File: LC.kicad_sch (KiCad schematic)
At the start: 81 parts, among them J1 INPUT+, J10 DISPLAY, J11 MODE_BUTTON, J12 CAL_BUTTON, J2 INPUT-, J3 Barrel_Jack, J4 EXT_CLK, J5 CLKSRC, J6 SIGSRC, J7 EXT_SIG, J8 Conn_01x06_Male, J9 PROG, Q1 BC817, Q2 BC817, SW1 RESET_BTN, U1 Omron_G2V, U10 74HC590PW,118, U11 74HCS251, U12 AVR32DB28x-xSO, U2 L7805, U3 74AHC1G04, U4 Omron_G2E, U5 74AHC1G14, U6 74AHC1G04, U7 LM311, U8 74AUC1G74, U9 74AUC2G125, Y1 10MHz

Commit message: update display connector
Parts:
- removed J10: DISPLAY, Connector_PinHeader_2.54mm:PinHeader_1x05_P2.54mm_Vertical, symbol Connector:Conn_01x05_Male
- added J10: DISPLAY, Connector_PinHeader_2.54mm:PinHeader_1x04_P2.54mm_Vertical, symbol Connector:Conn_01x04_Male
- renumbered C20 to C19, C21 to C20, C22 to C21, C23 to C22, C24 to C23, C25 to C24, C26 to C25, C27 to C26, C28 to C27
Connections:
- net +5V: now also J10.2 (Pin_2)
- net DISP/SDA: now also J10.3 (Pin_3)
- net DISP/SDC: now also J10.4 (Pin_4)
- net GND: now also J10.1 (Pin_1)
- net DISP/SS renamed UNUSED_6

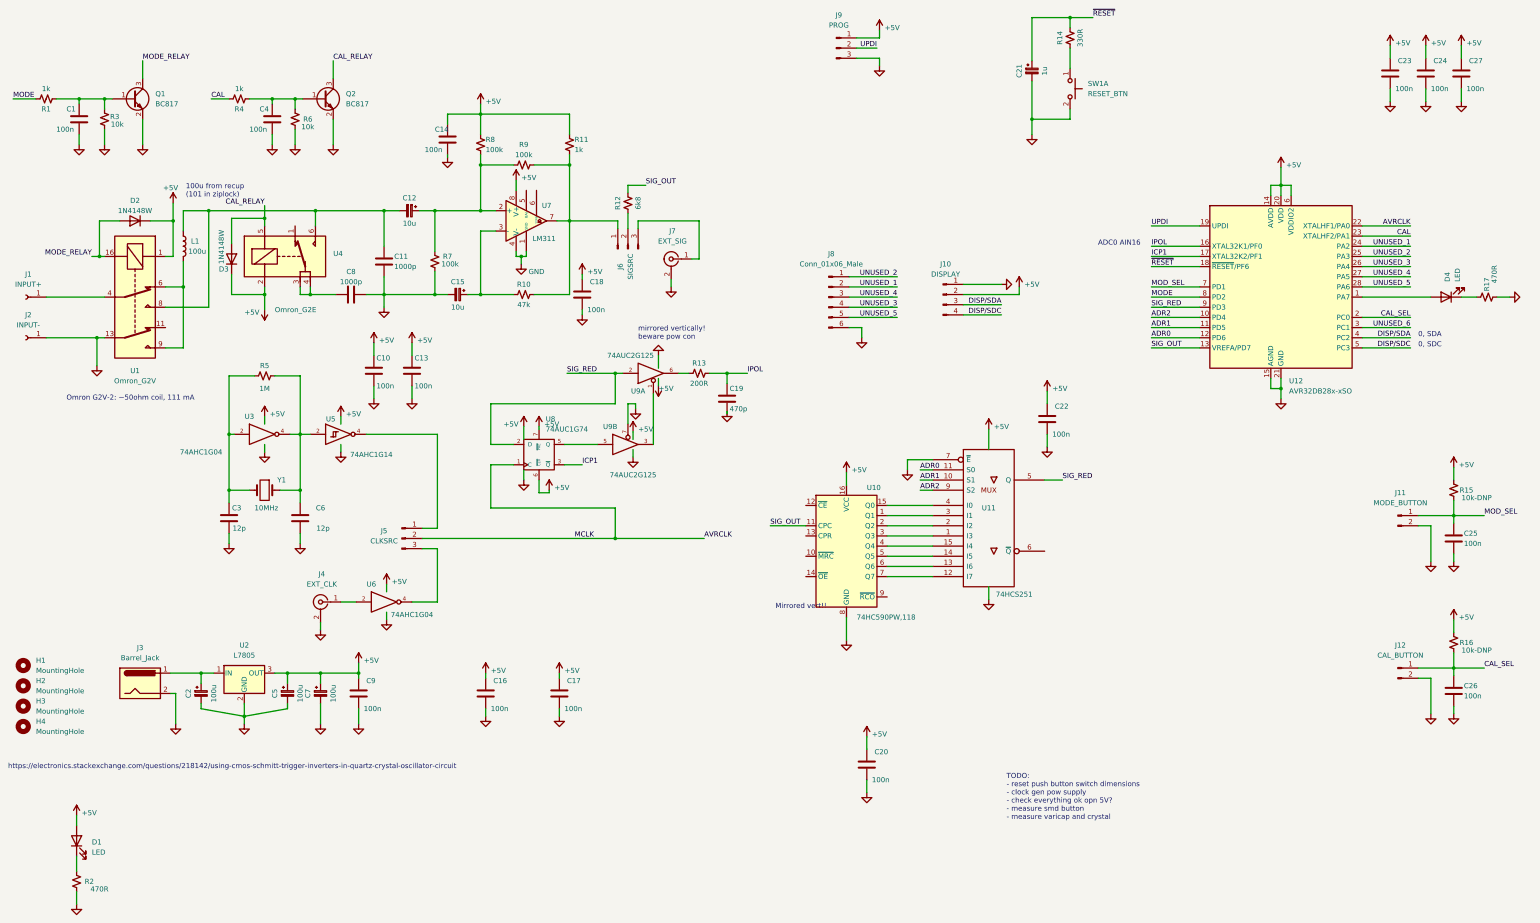
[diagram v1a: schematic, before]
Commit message: Unused IO to connector and LCD connector
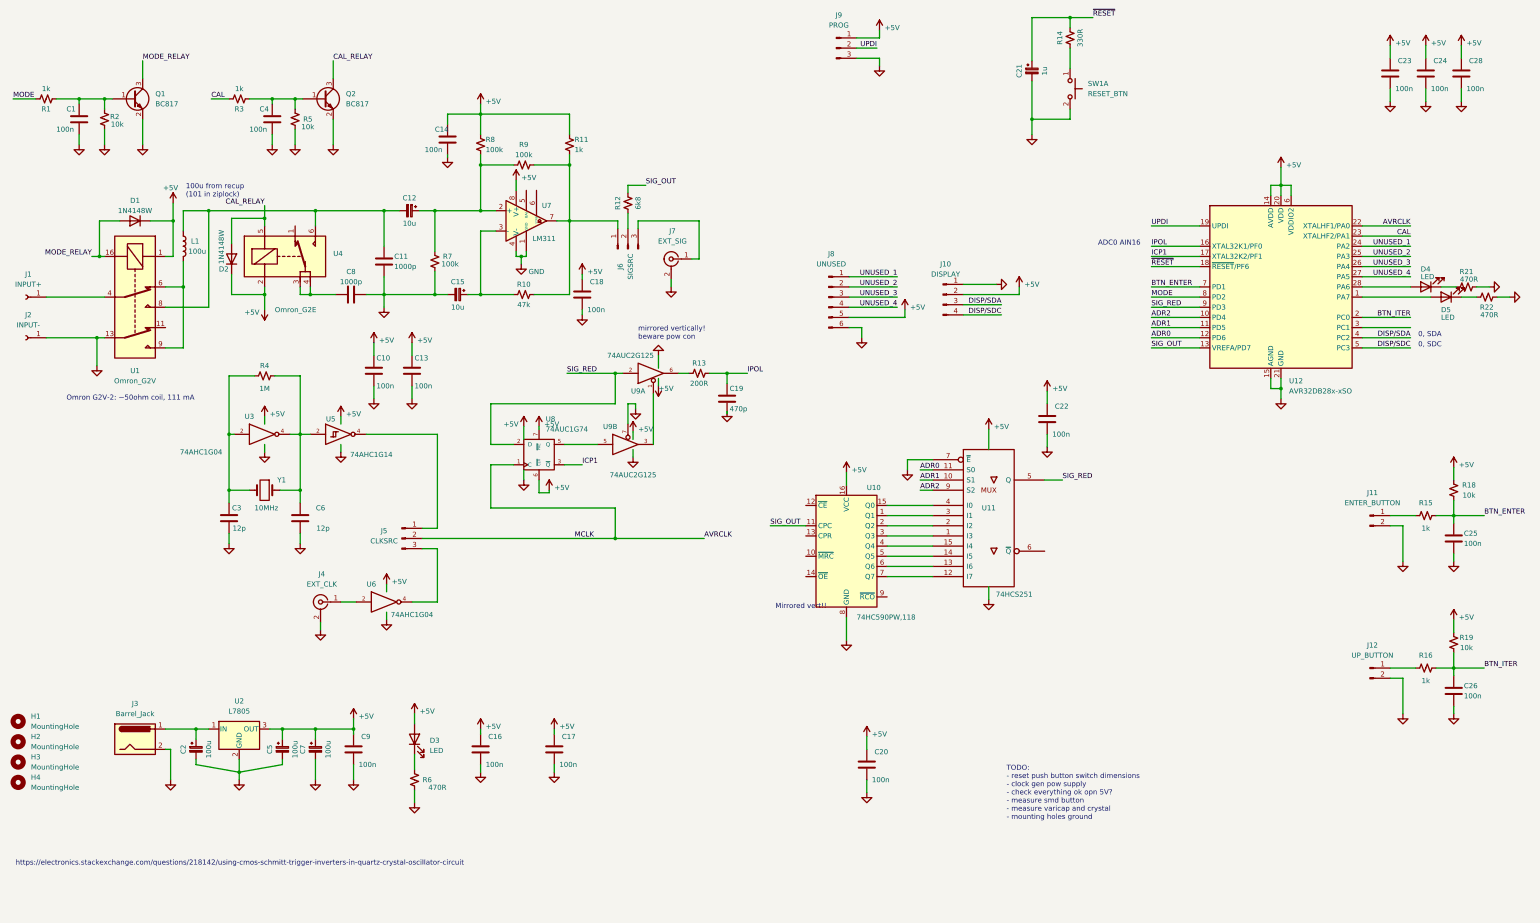
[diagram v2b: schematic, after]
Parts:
- added D4: LED, LED_SMD:LED_1206_3216Metric, symbol Device:LED
- added R15, R16: 1k, Resistor_SMD:R_0805_2012Metric_Pad1.20x1.40mm_HandSolder, symbol Device:R_Small_US
- added R21: 470R, Resistor_SMD:R_0805_2012Metric_Pad1.20x1.40mm_HandSolder, symbol Device:R_Small_US
- J11: value MODE_BUTTON -> ENTER_BUTTON
- J12: value CAL_BUTTON -> UP_BUTTON
- J8: value Conn_01x06_Male -> UNUSED
- R18: renamed from R15; value 10k-DNP -> 10k
- R19: renamed from R16; value 10k-DNP -> 10k
- renumbered C27 to C28, D2 to D1, D3 to D2, D1 to D3, D4 to D5, R3 to R2, R17 to R22, R4 to R3, R5 to R4, R6 to R5, R2 to R6
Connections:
- net +5V: now also J8.5 (Pin_5)
- net GND: now also R21.2
- net UNUSED_1: now also J8.1 (Pin_1); no longer J8.2 (Pin_2)
- net UNUSED_2: now also J8.2 (Pin_2); no longer J8.1 (Pin_1)
- net UNUSED_3: now also J8.3 (Pin_3); no longer J8.4 (Pin_4)
- net UNUSED_4: now also J8.4 (Pin_4); no longer J8.3 (Pin_3)
- net CAL_SEL renamed BTN_ITER
- net BTN_ITER: now also R16.2; no longer J12.1 (Pin_1)
- net MOD_SEL renamed BTN_ENTER
- net BTN_ENTER: now also R15.2; no longer J11.1 (Pin_1)
- net UNUSED_5: no longer names the net of U12.28 (PA6)
- net UNUSED_5: now also D4.2 (A); no longer J8.5 (Pin_5)
- net UNUSED_6: no longer names the net of U12.3 (PC1)
- new net: J12.1 (Pin_1), R16.1
- new net: J11.1 (Pin_1), R15.1
- new net: D4.1 (K), R21.1
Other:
- note added: "TODO: - reset push button switch dimensions - clock gen pow supply - check everything ok opn 5V? - measure smd button - measure varicap and crystal - mounting holes ground"
- note removed: "TODO: - reset push button switch dimensions - clock gen pow supply - check everything ok opn 5V? - measure smd button - measure varicap and crystal"
- moved on the sheet: C16, C17, C2, C5, C7, C9, D3, H1, H2, H3, H4, J11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

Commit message: update gitignore and init code
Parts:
- added TP1: TestPoint, TestPoint:TestPoint_THTPad_1.0x1.0mm_Drill0.5mm, symbol Connector:TestPoint
- renumbered C28 to C27, R18 to R17, R19 to R18, R21 to R19, R22 to R20
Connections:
- net LED_2: now reaches D5.2 (A), U12.1 (PA7)
- net LED_1: now reaches D4.2 (A), U12.28 (PA6)
- net UNUSED_5: now reaches U12.3 (PC1)
- net UNUSED_5: now also TP1.1

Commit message: changed comparator: LM311 became TLV3201
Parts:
- removed U7: LM311, Package_SO:SOIC-8-1EP_3.9x4.9mm_P1.27mm_EP2.41x3.3mm, symbol Comparator:LM311
- added U10: TLV3201, Package_TO_SOT_SMD:SOT-23-5, symbol Comparator:TLV7031DBV
- renumbered U10 to U11, U11 to U12, U12 to U13
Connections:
- net +5V: now also U10.5 (V+)
- net GND: now also U10.2 (V-)
- net IN+: now reaches C12.1, R7.2, R8.1, R9.1
- net IN+: now also U10.3 (+)
- net IN-: now reaches C15.1, R10.1
- net IN-: now also U10.4 (-)
- net COMP_OUT: now reaches J6.1 (Pin_1), R10.2, R11.1, R9.2
- net COMP_OUT: now also U10.1
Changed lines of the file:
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@@
   (junction (at 93.98 66.675) (diameter 0) (color 0 0 0 0)
   )
-  (junction (at 145.415 78.105) (diameter 0) (color 0 0 0 0)
-  )
   (junction (at 123.825 66.675) (diameter 0) (color 0 0 0 0)
   )
@@
     (stroke (width 0) (type default) (color 0 0 0 0))
   )
-  (wire (pts (xy 146.685 78.105) (xy 145.415 78.105))
-    (stroke (width 0) (type default) (color 0 0 0 0))
-  )
   (wire (pts (xy 187.96 78.74) (xy 189.865 78.74))
     (stroke (width 0) (type default) (color 0 0 0 0))
@@
     (stroke (width 0) (type default) (color 0 0 0 0))
   )
-  (wire (pts (xy 145.415 78.105) (xy 144.145 78.105))
-    (stroke (width 0) (type default) (color 0 0 0 0))
-  )
   (wire (pts (xy 85.725 203.835) (xy 85.725 205.105))
     (stroke (width 0) (type default) (color 0 0 0 0))
@@
     (stroke (width 0) (type default) (color 0 0 0 0))
   )
-  (wire (pts (xy 145.415 78.105) (xy 145.415 80.01))
+  (wire (pts (xy 144.145 76.835) (xy 144.145 78.74))
     (stroke (width 0) (type default) (color 0 0 0 0))
   )
@@
     (stroke (width 0) (type default) (color 0 0 0 0))
   )
-  (wire (pts (xy 144.145 78.105) (xy 144.145 76.835))
-    (stroke (width 0) (type default) (color 0 0 0 0))
-  )
   (wire (pts (xy 367.665 78.105) (xy 355.6 78.105))
     (stroke (width 0) (type default) (color 0 0 0 0))
@@
     (stroke (width 0) (type default) (color 0 0 0 0))
   )
-  (wire (pts (xy 146.685 76.835) (xy 146.685 78.105))
-    (stroke (width 0) (type default) (color 0 0 0 0))
-  )
   (wire (pts (xy 239.395 88.265) (xy 227.33 88.265))
     (stroke (width 0) (type default) (color 0 0 0 0))
@@
     (effects (font (size 1.27 1.27)) (justify left bottom))
   )
+  (label "IN-" (at 136.525 71.755 0)
+    (effects (font (size 1.27 1.27)) (justify left bottom))
+  )
   (label "SIG_OUT" (at 176.53 60.325 0)
     (effects (font (size 1.27 1.27)) (justify left bottom))
@@
     (effects (font (size 1.27 1.27)) (justify left bottom))
   )
+  (label "IN+" (at 136.525 66.675 0)
+    (effects (font (size 1.27 1.27)) (justify left bottom))
+  )
   (label "UNUSED_1" (at 367.665 75.565 180)
     (effects (font (size 1.27 1.27)) (justify right bottom))
@@
     (effects (font (size 1.27 1.27)) (justify right bottom))
   )
+  (label "COMP_OUT" (at 154.94 69.215 0)
+    (effects (font (size 1.27 1.27)) (justify left bottom))
+  )
   (label "MODE_RELAY" (at 38.1 78.105 180)
     (effects (font (size 1.27 1.27)) (justify right bottom))
@@
     (pin "1")
   )
-  (symbol (lib_id "power:GND") (at 145.415 80.01 0) (unit 1)
+  (symbol (lib_id "power:GND") (at 144.145 78.74 0) (unit 1)
     (in_bom yes) (on_board yes)
-    (property "Reference" "#PWR036" (id 0) (at 145.415 86.36 0)
+    (property "Reference" "#PWR036" (id 0) (at 144.145 85.09 0)
       (effects (font (size 1.27 1.27)) hide)
     )
-    (property "Value" "GND" (id 1) (at 149.225 81.915 0))
-    (property "Footprint" "" (id 2) (at 145.415 80.01 0)
+    (property "Value" "GND" (id 1) (at 147.955 80.645 0))
+    (property "Footprint" "" (id 2) (at 144.145 78.74 0)
       (effects (font (size 1.27 1.27)) hide)
     )
-    (property "Datasheet" "" (id 3) (at 145.415 80.01 0)
+    (property "Datasheet" "" (id 3) (at 144.145 78.74 0)
       (effects (font (size 1.27 1.27)) hide)
     )
@@
   (symbol (lib_id "74xx_IEEE:74251") (at 262.255 142.875 0) (unit 1)
     (in_bom yes) (on_board yes)
-    (property "Reference" "U11" (id 0) (at 262.255 140.97 0))
+    (property "Reference" "U12" (id 0) (at 262.255 140.97 0))
     (property "Value" "74HCS251" (id 1) (at 268.605 162.56 0))
     (property "Footprint" "Package_SO:SOIC-16_4.55x10.3mm_P1.27mm" (id 2) (at 262.255 142.875 0)
@@
     (pin "2")
   )
+  (symbol (lib_id "Comparator:TLV7031DBV") (at 146.685 69.215 0) (unit 1)
+    (in_bom yes) (on_board yes)
+    (property "Reference" "U10" (id 0) (at 146.685 61.595 0))
+    (property "Value" "TLV3201" (id 1) (at 149.225 64.135 0))
+    (property "Footprint" "Package_TO_SOT_SMD:SOT-23-5" (id 2) (at 144.145 74.295 0)
+      (effects (font (size 1.27 1.27)) (justify left) hide)
+    )
+    (property "Datasheet" "https://www.ti.com/lit/ds/symlink/tlv7031.pdf" (id 3) (at 146.685 64.135 0)
+      (effects (font (size 1.27 1.27)) hide)
+    )
+    (pin "2")
+    (pin "5")
+    (pin "1")
+    (pin "3")
+    (pin "4")
+  )
   (symbol (lib_id "Device:C_Polarized_Small") (at 117.475 66.675 270) (unit 1)
     (in_bom yes) (on_board yes)
@@
   (symbol (lib_id "MCU_Microchip_AVR_Dx:AVR32DB28x-xSO") (at 335.28 85.725 0) (unit 1)
     (in_bom yes) (on_board yes) (fields_autoplaced)
-    (property "Reference" "U12" (id 0) (at 337.2994 109.22 0)
+    (property "Reference" "U13" (id 0) (at 337.2994 109.22 0)
       (effects (font (size 1.27 1.27)) (justify left))
     )
@@
   (symbol (lib_id "74xx:74HC590") (at 226.695 153.035 0) (unit 1)
     (in_bom yes) (on_board yes)
-    (property "Reference" "U10" (id 0) (at 231.775 135.89 0)
+    (property "Reference" "U11" (id 0) (at 231.775 135.89 0)
       (effects (font (size 1.27 1.27)) (justify left))
     )
@@
     (pin "1")
   )
-  (symbol (lib_id "Comparator:LM311") (at 146.685 69.215 0) (unit 1)
-    (in_bom yes) (on_board yes)
-    (property "Reference" "U7" (id 0) (at 151.765 65.405 0))
-    (property "Value" "LM311" (id 1) (at 151.13 73.66 0))
-    (property "Footprint" "Package_SO:SOIC-8-1EP_3.9x4.9mm_P1.27mm_EP2.41x3.3mm" (id 2) (at 146.685 69.215 0)
-      (effects (font (size 1.27 1.27)) hide)
-    )
-    (property "Datasheet" "https://www.st.com/resource/en/datasheet/lm311.pdf" (id 3) (at 146.685 69.215 0)
-      (effects (font (size 1.27 1.27)) hide)
-    )
-    (pin "1")
-    (pin "2")
-    (pin "3")
-    (pin "4")
-    (pin "5")
-    (pin "6")
-    (pin "7")
-    (pin "8")
-  )
   (symbol (lib_id "power:+5V") (at 152.4 136.525 0) (unit 1)
     (in_bom yes) (on_board yes)
@@
       (reference "U6") (unit 1) (value "74AHC1G04") (footprint "Package_TO_SOT_SMD:SOT-23-5_HandSoldering")
     )
-    (path "/e2f067f1-c989-43ab-9cfa-23c1f9e18b39"
-      (reference "U7") (unit 1) (value "LM311") (footprint "Package_SO:SOIC-8-1EP_3.9x4.9mm_P1.27mm_EP2.41x3.3mm")
-    )
     (path "/bdc82b14-9cfe-4a26-bfe3-09c093fb2345"
       (reference "U8") (unit 1) (value "74AUC1G74") (footprint "Package_SO:VSSOP-8_2.3x2mm_P0.5mm")
@@
       (reference "U9") (unit 2) (value "74AUC2G125") (footprint "Package_SO:VSSOP-8_2.4x2.1mm_P0.5mm")
     )
+    (path "/1aff49b6-bd0b-404b-bd3a-71b68a68ad3b"
+      (reference "U10") (unit 1) (value "TLV3201") (footprint "Package_TO_SOT_SMD:SOT-23-5")
+    )
     (path "/be55dabe-c026-4082-96e0-5f65c839136b"
-      (reference "U10") (unit 1) (value "74HC590PW,118") (footprint "Package_SO:TSSOP-16_4.4x5mm_P0.65mm")
+      (reference "U11") (unit 1) (value "74HC590PW,118") (footprint "Package_SO:TSSOP-16_4.4x5mm_P0.65mm")
     )
     (path "/10bd52e6-af6a-413e-9c10-f3da44c4133b"
-      (reference "U11") (unit 1) (value "74HCS251") (footprint "Package_SO:SOIC-16_4.55x10.3mm_P1.27mm")
+      (reference "U12") (unit 1) (value "74HCS251") (footprint "Package_SO:SOIC-16_4.55x10.3mm_P1.27mm")
     )
     (path "/8b3913bb-73bc-468d-a4a4-eaf44e1d1389"
-      (reference "U12") (unit 1) (value "AVR32DB28x-xSO") (footprint "Package_SO:SOIC-28W_7.5x17.9mm_P1.27mm")
+      (reference "U13") (unit 1) (value "AVR32DB28x-xSO") (footprint "Package_SO:SOIC-28W_7.5x17.9mm_P1.27mm")
     )
     (path "/933c2574-012e-47d3-94dd-3c3fcd695e78"

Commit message: R11 is Do Not Populate
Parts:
- R11: value 1k -> 1k DNP
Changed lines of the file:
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@@
       (effects (font (size 1.27 1.27)) (justify right))
     )
-    (property "Value" "1k" (id 1) (at 158.75 51.435 0)
+    (property "Value" "1k DNP" (id 1) (at 158.75 51.435 0)
       (effects (font (size 1.27 1.27)) (justify right))
     )
@@
     )
     (path "/bc1ca884-2afd-42a1-8548-cfe1cb2875a3"
-      (reference "R11") (unit 1) (value "1k") (footprint "Resistor_SMD:R_0805_2012Metric_Pad1.20x1.40mm_HandSolder")
+      (reference "R11") (unit 1) (value "1k DNP") (footprint "Resistor_SMD:R_0805_2012Metric_Pad1.20x1.40mm_HandSolder")
     )
     (path "/2a461ff4-590b-454e-9023-8769a68e7daa"

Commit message: Updated comparator oscillator with LTSpice simulation results
LT1719 operates nicely, but some values need to be adjusted. Especially the coupling caps need to be changed (10u -> 1u) so I decided to change them to MLCC.
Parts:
- removed C12, C15: 10u, Capacitor_THT:CP_Radial_D5.0mm_P2.00mm, symbol Device:C_Polarized_Small
- removed U10: TLV3201, Package_TO_SOT_SMD:SOT-23-5, symbol Comparator:TLV7031DBV
- added C12, C15: 1u, Capacitor_SMD:C_0805_2012Metric_Pad1.18x1.45mm_HandSolder, symbol Device:C
- added U7: LT1719CS6, Package_TO_SOT_SMD_AKL:SOT-23-6, symbol Analog_Comparator_AKL:LT1719CS6
- R10: value 47k -> 68k
- R8, R9: value 100k -> 120k
- renumbered U11 to U10, U12 to U11, U13 to U12
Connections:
- net +5V: now also U7.4 (V+)
- net GND: now also C15.1, U7.2 (V-), U7.6 (SHDN)
- net SIG_OUT: now also J6.2 (Pin_2); no longer R12.2
- net at C11.2, L1.1, U1.8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: now also C12.1
- net at R12.1: now also J6.1 (Pin_1); no longer J6.2 (Pin_2)
- net COMP_OUT: no longer names the net of R10.2, R11.1, R9.2
- net COMP_OUT: now also R12.2, U7.5; no longer J6.1 (Pin_1)
- net IN+: no longer names the net of R7.2, R8.1, R9.1
- net IN+: now also C12.2, U7.3 (+)
- net IN-: no longer names the net of R10.1
- net IN-: now also C15.2, U7.1 (-)
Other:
- note added: "TODO: - check everything ok opn 5V? - measure varicap and crystal - mounting holes ground"
- note removed: "TODO: - reset push button switch dimensions - clock gen pow supply - check everything ok opn 5V? - measure smd button - measure varicap and crystal - mounting holes ground"
- moved on the sheet: J6, J7, R12
